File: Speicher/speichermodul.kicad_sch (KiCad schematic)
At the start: 69 parts, among them IC1 6116, J1 Conn_01x02, J2 Conn_01x02, J3 Conn_01x02, P1 CONN_3X2, P8 CONN_02X10, P9 CONN_02X10, SW1 Digitast rot, SW2 Digitast grün, U1 74HC00, U2 74HC08, U3 74HC14, U4 74HC14, U5 74LS540, U6 74LS540

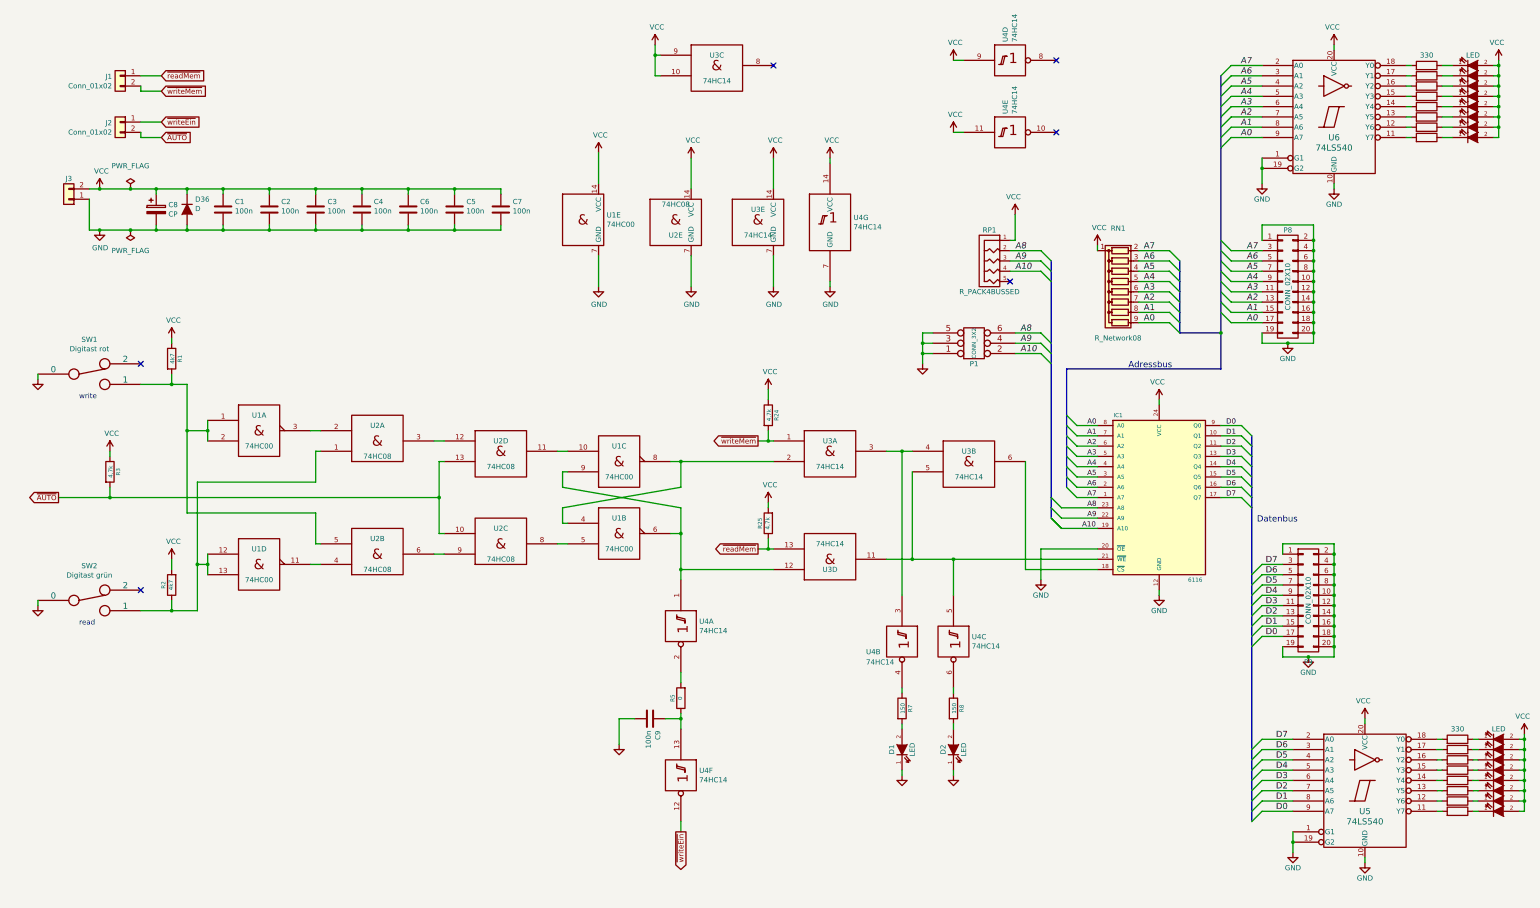
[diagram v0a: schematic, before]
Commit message: - Werte von Bauteilen in den Schaltplänen ergänzt - weitere Hinweise zum Nachbau
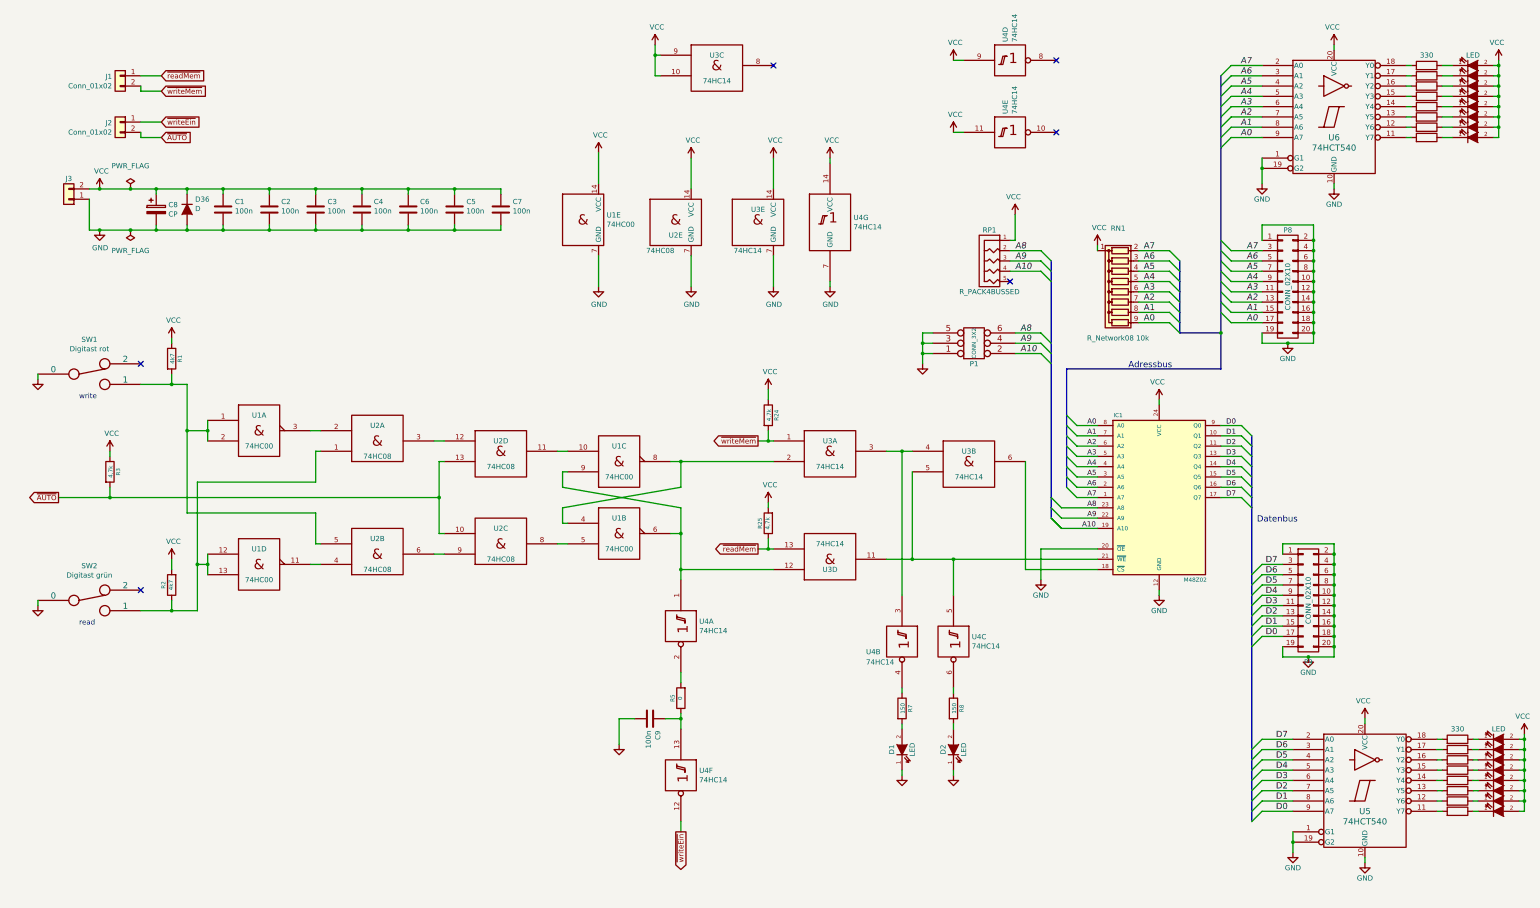
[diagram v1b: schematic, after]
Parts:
- IC1: value 6116 -> M48Z02
- RN1: value R_Network08 -> R_Network08 10k
- U5, U6: value 74LS540 -> 74HCT540

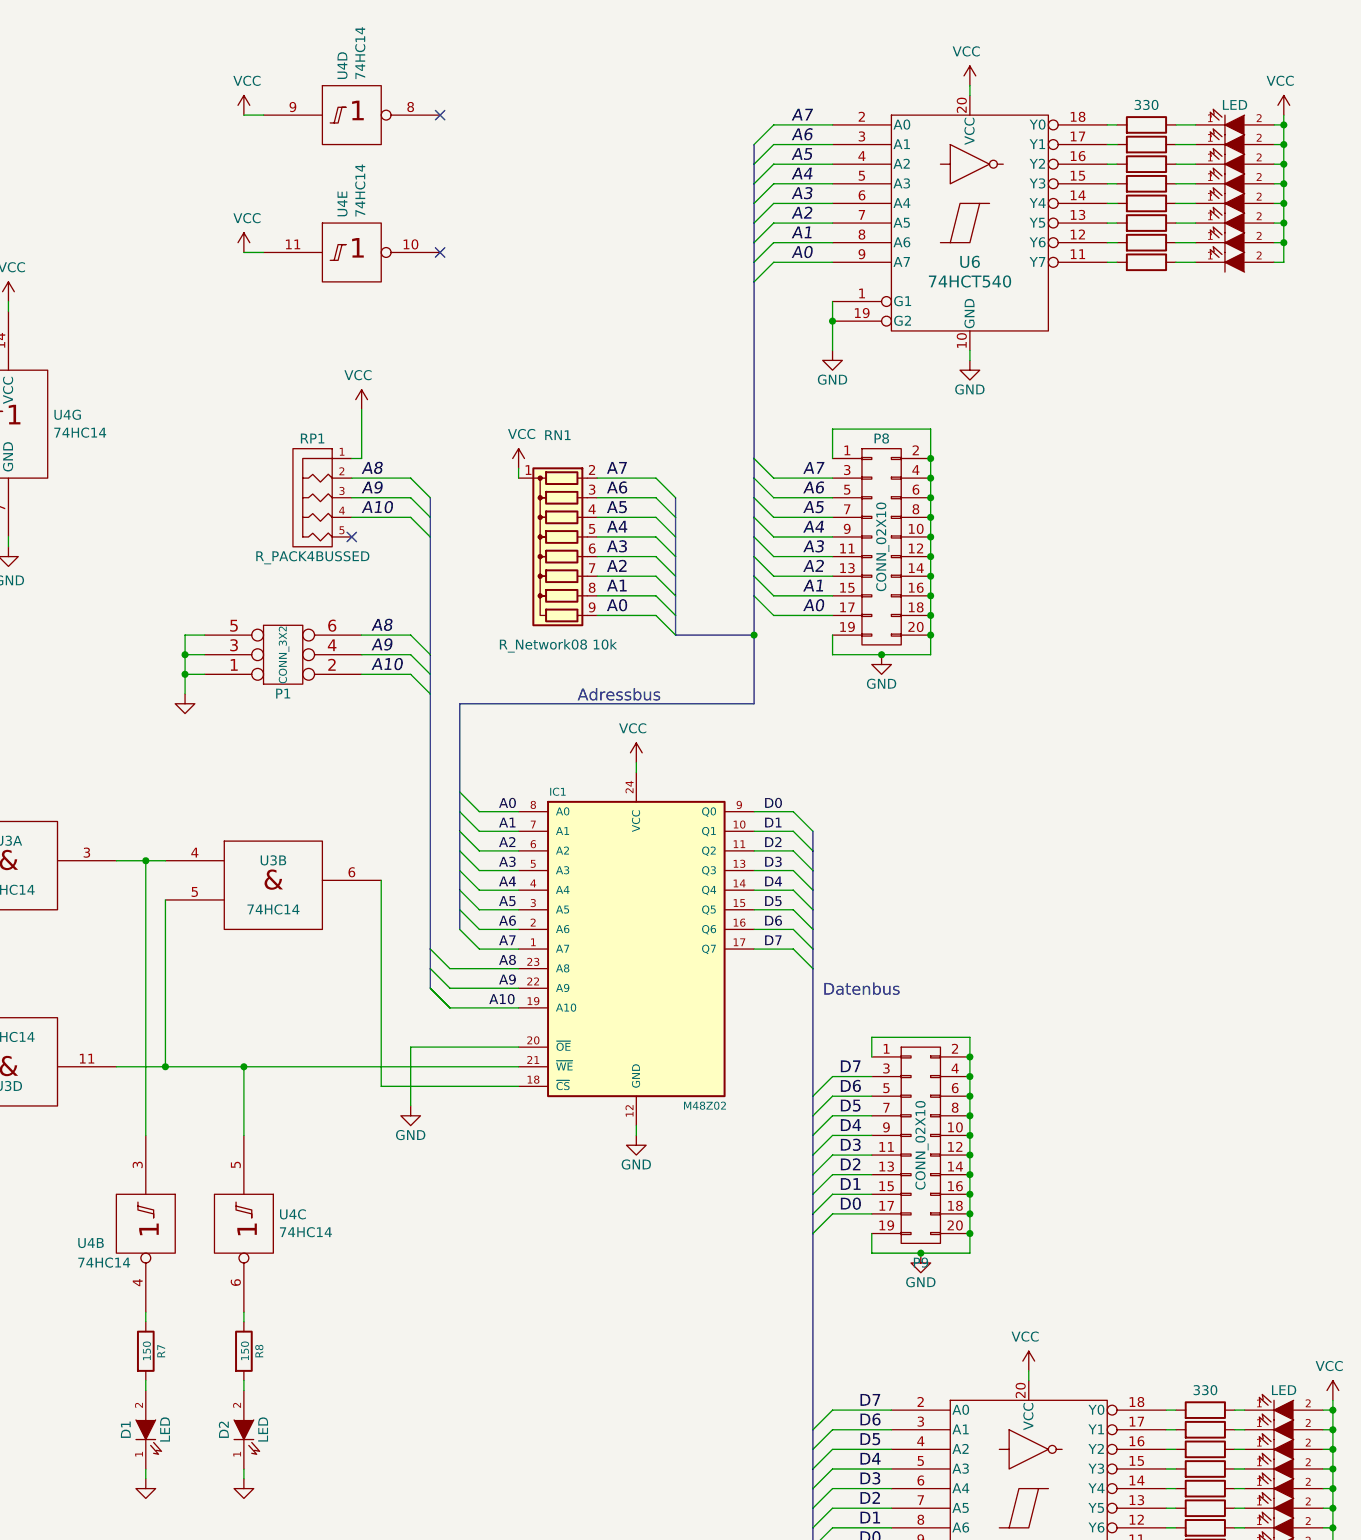
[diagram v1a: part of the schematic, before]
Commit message: Alle Vorwiderstände vor LEDs in 680 Ohm geändert (Issue 5)
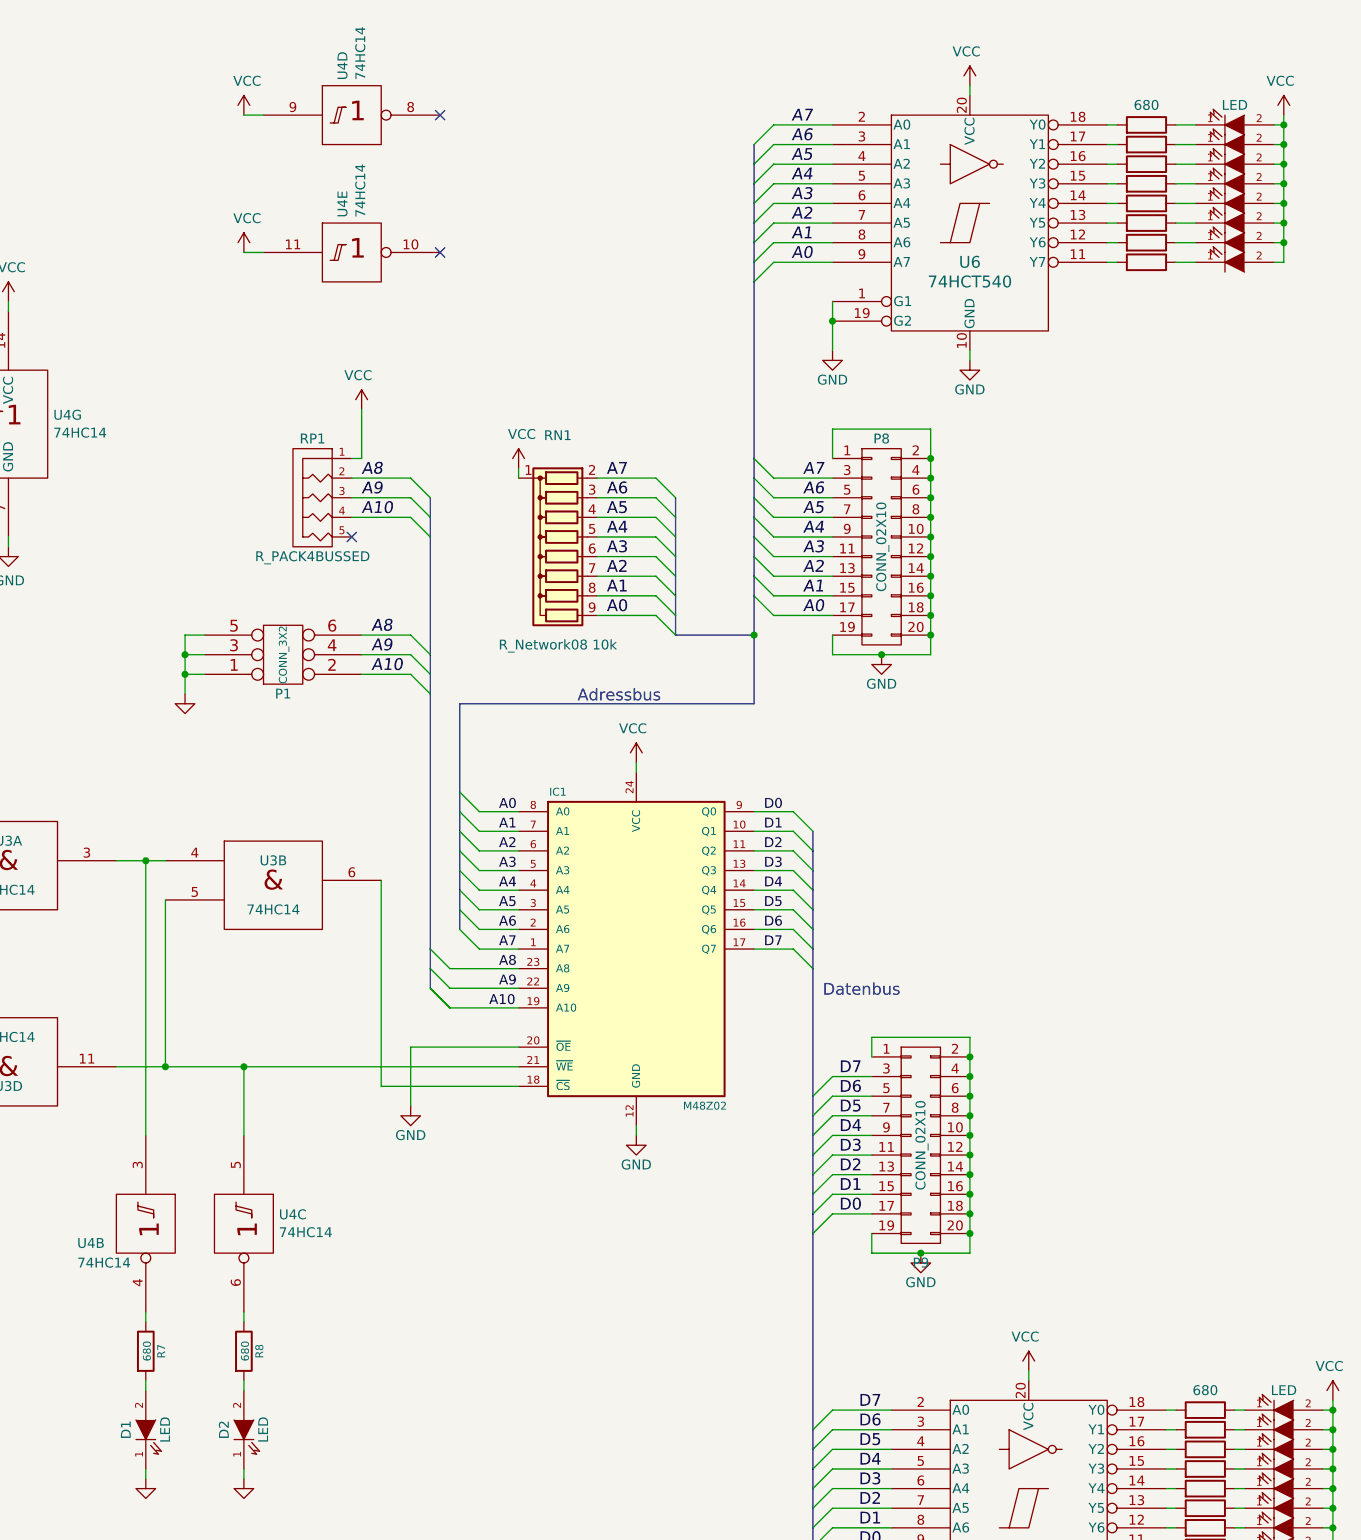
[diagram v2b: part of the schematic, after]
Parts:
- R10, R11, R12, R13, R14, R15, R16, R17, R18, R19, R20, R21, R22, R23, R4, R9: value 330 -> 680
- R7, R8: value 150 -> 680
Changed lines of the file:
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@@
       (effects (font (size 1.016 1.016)))
     )
-    (property "Value" "150" (at 230.0478 203.1746 90)
+    (property "Value" "680" (at 230.0478 203.1746 90)
       (effects (font (size 1.016 1.016)))
     )
@@
       (effects (font (size 1.016 1.016)))
     )
-    (property "Value" "150" (at 242.7478 203.1746 90)
+    (property "Value" "680" (at 242.7478 203.1746 90)
       (effects (font (size 1.016 1.016)))
     )
@@
       (effects (font (size 1.27 1.27)) hide)
     )
-    (property "Value" "330" (at 367.03 208.28 90)
+    (property "Value" "680" (at 367.03 208.28 90)
       (effects (font (size 1.27 1.27)))
     )
@@
       (effects (font (size 1.27 1.27)) hide)
     )
-    (property "Value" "330" (at 367.03 213.36 90)
+    (property "Value" "680" (at 367.03 213.36 90)
       (effects (font (size 1.27 1.27)) hide)
     )
@@
       (effects (font (size 1.27 1.27)) hide)
     )
-    (property "Value" "330" (at 367.03 215.9 90)
+    (property "Value" "680" (at 367.03 215.9 90)
       (effects (font (size 1.27 1.27)) hide)
     )
@@
       (effects (font (size 1.27 1.27)) hide)
     )
-    (property "Value" "330" (at 367.03 218.44 90)
+    (property "Value" "680" (at 367.03 218.44 90)
       (effects (font (size 1.27 1.27)) hide)
     )
@@
       (effects (font (size 1.27 1.27)) hide)
     )
-    (property "Value" "330" (at 367.03 220.98 90)
+    (property "Value" "680" (at 367.03 220.98 90)
       (effects (font (size 1.27 1.27)) hide)
     )
@@
       (effects (font (size 1.27 1.27)) hide)
     )
-    (property "Value" "330" (at 367.03 223.52 90)
+    (property "Value" "680" (at 367.03 223.52 90)
       (effects (font (size 1.27 1.27)) hide)
     )
@@
       (effects (font (size 1.27 1.27)) hide)
     )
-    (property "Value" "330" (at 367.03 226.06 90)
+    (property "Value" "680" (at 367.03 226.06 90)
       (effects (font (size 1.27 1.27)) hide)
     )
@@
       (effects (font (size 1.27 1.27)) hide)
     )
-    (property "Value" "330" (at 367.03 231.14 90)
+    (property "Value" "680" (at 367.03 231.14 90)
       (effects (font (size 1.27 1.27)) hide)
     )
@@
       (effects (font (size 1.27 1.27)) hide)
     )
-    (property "Value" "330" (at 359.41 41.91 90)
+    (property "Value" "680" (at 359.41 41.91 90)
       (effects (font (size 1.27 1.27)))
     )
@@
       (effects (font (size 1.27 1.27)) hide)
     )
-    (property "Value" "330" (at 359.41 46.99 90)
+    (property "Value" "680" (at 359.41 46.99 90)
       (effects (font (size 1.27 1.27)) hide)
     )
@@
       (effects (font (size 1.27 1.27)) hide)
     )
-    (property "Value" "330" (at 359.41 49.53 90)
+    (property "Value" "680" (at 359.41 49.53 90)
       (effects (font (size 1.27 1.27)) hide)
     )
@@
       (effects (font (size 1.27 1.27)) hide)
     )
-    (property "Value" "330" (at 359.41 52.07 90)
+    (property "Value" "680" (at 359.41 52.07 90)
       (effects (font (size 1.27 1.27)) hide)
     )
@@
       (effects (font (size 1.27 1.27)) hide)
     )
-    (property "Value" "330" (at 359.41 54.61 90)
+    (property "Value" "680" (at 359.41 54.61 90)
       (effects (font (size 1.27 1.27)) hide)
     )
@@
       (effects (font (size 1.27 1.27)) hide)
     )
-    (property "Value" "330" (at 359.41 57.15 90)
+    (property "Value" "680" (at 359.41 57.15 90)
       (effects (font (size 1.27 1.27)) hide)
     )
@@
       (effects (font (size 1.27 1.27)) hide)
     )
-    (property "Value" "330" (at 359.41 59.69 90)
+    (property "Value" "680" (at 359.41 59.69 90)
       (effects (font (size 1.27 1.27)) hide)
     )
@@
       (effects (font (size 1.27 1.27)) hide)
     )
-    (property "Value" "330" (at 359.41 62.23 90)
-      (effects (font (size 1.27 1.27)) hide)
-    )
+    (property "Value" "680" (at 359.41 62.23 90)
+      (effects (font (size 1.27 1.27)) hide)
+    )
